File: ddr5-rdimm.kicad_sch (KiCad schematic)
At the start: 34 parts, among them J2 Bus_DDR5_DDR504111002KQ, Q10 BSS138PW, Q11 BSS138PW, Q23 SI7613DN-T1-GE3, Q25 BSS138PW, Q26 BSS138PW, Q27 SI7613DN-T1-GE3, Q9 BSS138PW, SW3 SW_KMR211NGLFS_SMD

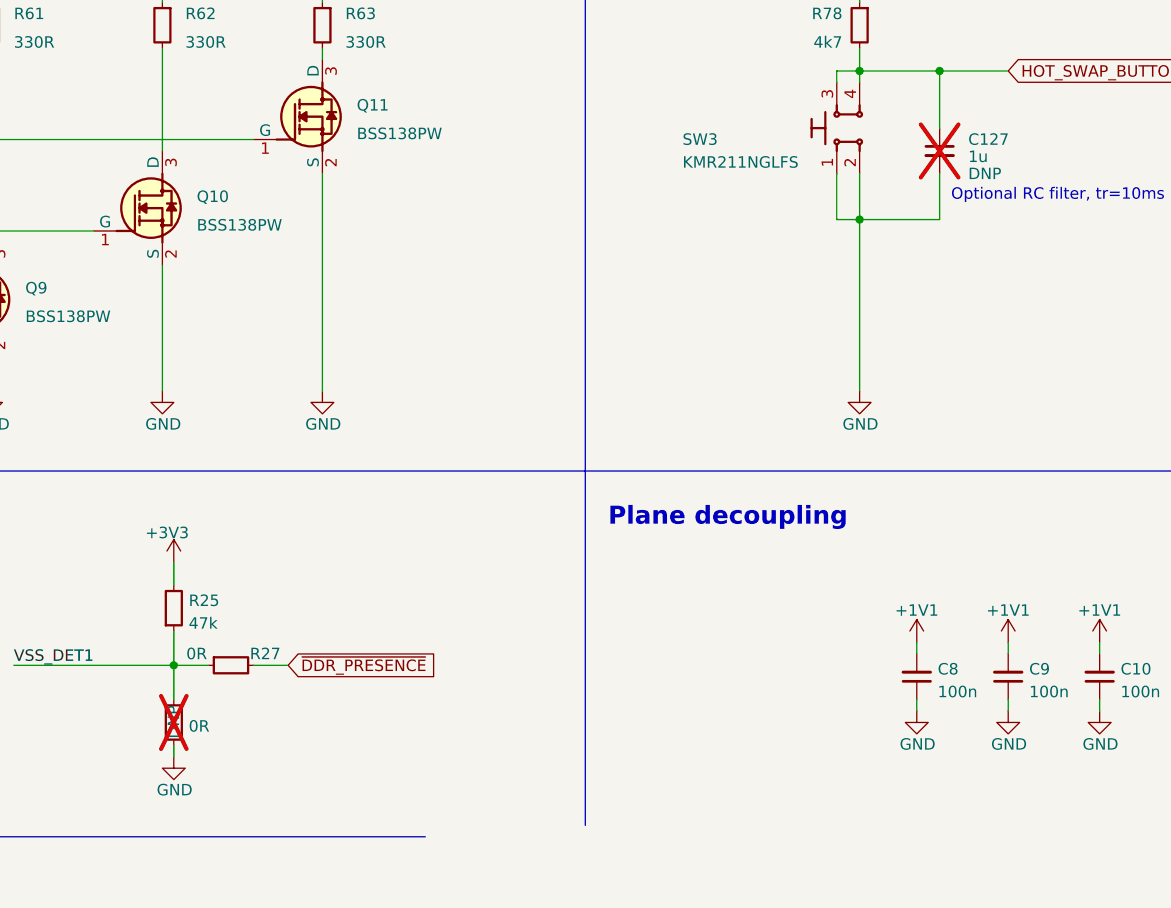
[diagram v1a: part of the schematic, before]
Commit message: [#69629] Fix DNP attributes
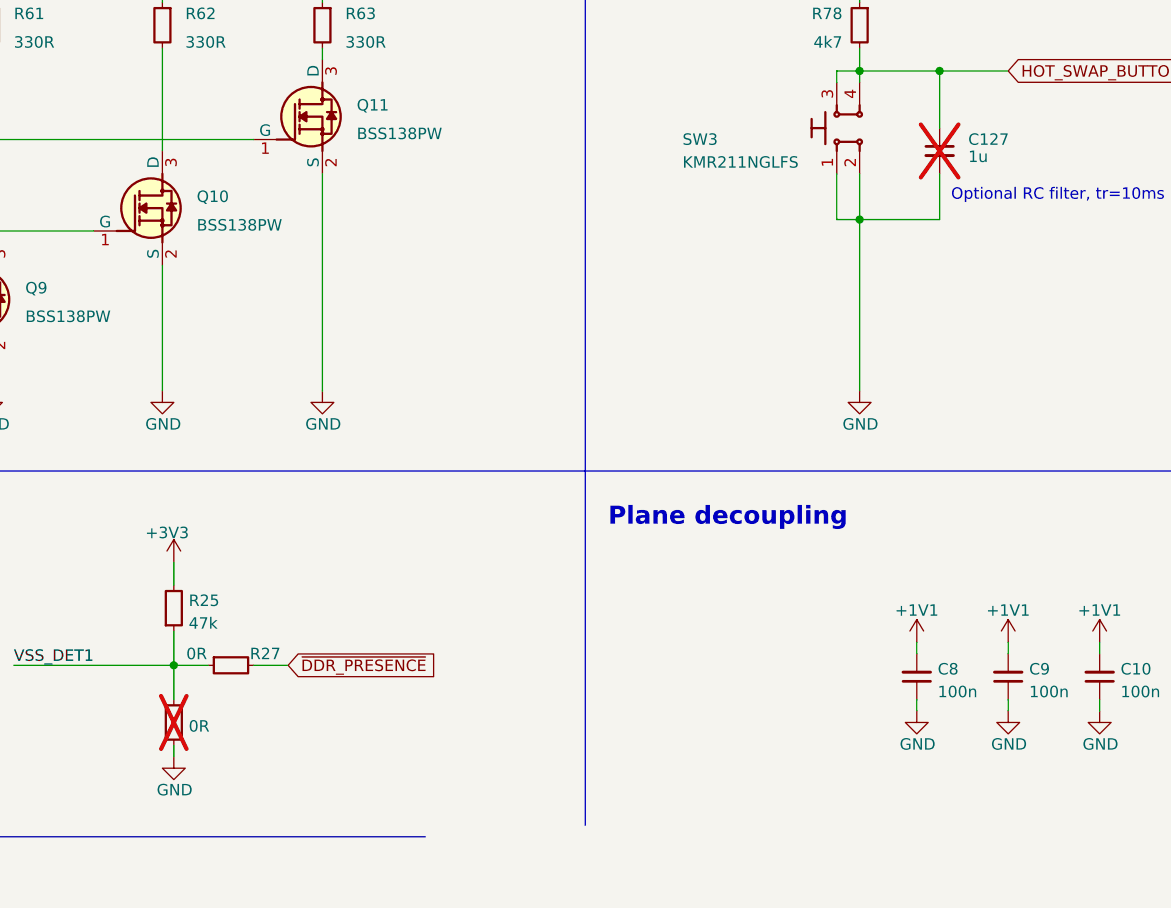
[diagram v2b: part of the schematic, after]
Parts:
- C127, R26: DNP DNP -> (none)

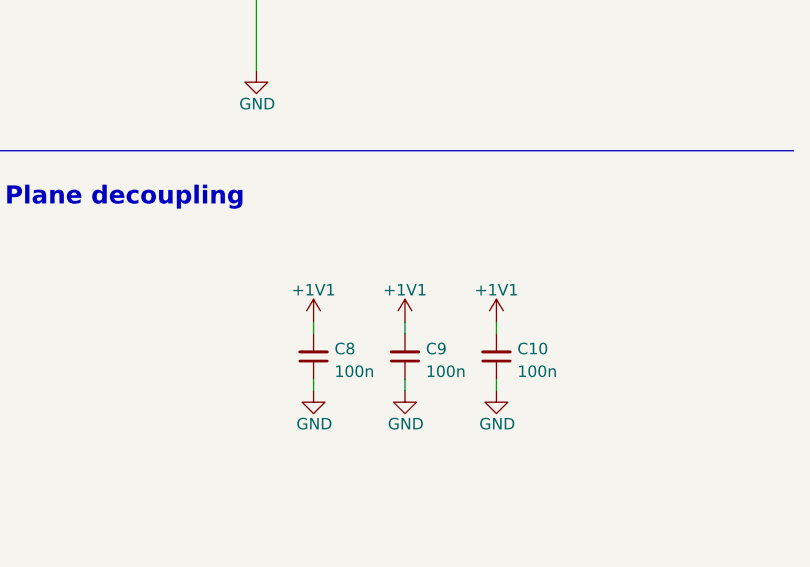
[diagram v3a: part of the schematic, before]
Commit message: [#70235] Improve power supply labels
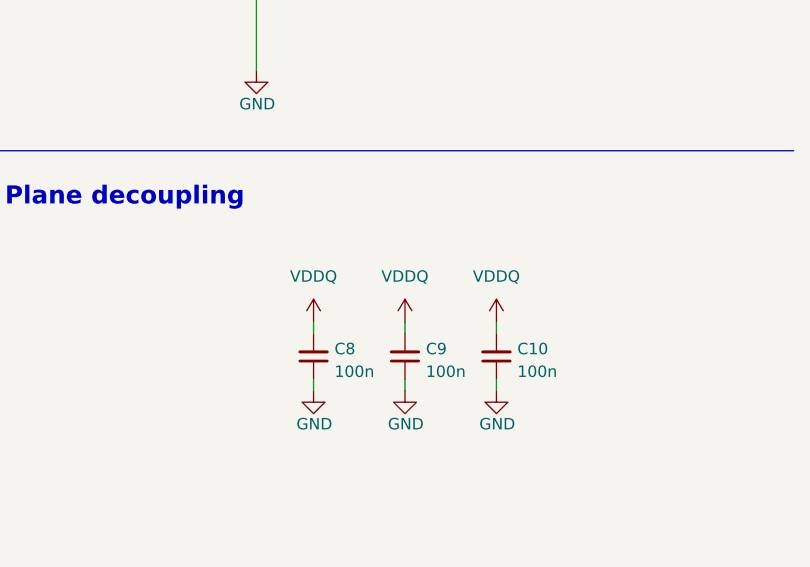
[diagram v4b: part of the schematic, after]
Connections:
- net +1V1 renamed VDDQ
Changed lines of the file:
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@@
 	)
 	(symbol
+		(lib_id "antmicropower:VDD")
+		(at 374.65 232.41 0)
+		(unit 1)
+		(exclude_from_sim no)
+		(in_bom yes)
+		(on_board yes)
+		(dnp no)
+		(fields_autoplaced yes)
+		(property "Reference" "#PWR0117"
+			(at 374.65 236.22 0)
+			(effects
+				(font
+					(size 1.27 1.27)
+				)
+				(hide yes)
+			)
+		)
+		(property "Value" "VDDQ"
+			(at 374.65 227.33 0)
+			(effects
+				(font
+					(size 1.27 1.27)
+				)
+			)
+		)
+		(property "Footprint" ""
+			(at 374.65 232.41 0)
+			(effects
+				(font
+					(size 1.27 1.27)
+				)
+				(hide yes)
+			)
+		)
+		(property "Datasheet" ""
+			(at 374.65 232.41 0)
+			(effects
+				(font
+					(size 1.27 1.27)
+				)
+				(hide yes)
+			)
+		)
+		(property "Description" ""
+			(at 374.65 232.41 0)
+			(effects
+				(font
+					(size 1.27 1.27)
+				)
+				(hide yes)
+			)
+		)
+		(pin "1"
+		)
+		(instances
+			(project "data-center-rdimm-ddr5-tester"
+				(path "/1faa6543-e26a-4449-8bac-ee14b9f19e5f/00000000-0000-0000-0000-000061827943"
+					(reference "#PWR0117")
+					(unit 1)
+				)
+			)
+		)
+	)
+	(symbol
 		(lib_id "antmicroResistors0402:R_330R_0402")
 		(at 270.51 161.29 270)
@@
 	)
 	(symbol
+		(lib_id "antmicropower:VDD")
+		(at 364.49 232.41 0)
+		(unit 1)
+		(exclude_from_sim no)
+		(in_bom yes)
+		(on_board yes)
+		(dnp no)
+		(fields_autoplaced yes)
+		(property "Reference" "#PWR044"
+			(at 364.49 236.22 0)
+			(effects
+				(font
+					(size 1.27 1.27)
+				)
+				(hide yes)
+			)
+		)
+		(property "Value" "VDDQ"
+			(at 364.49 227.33 0)
+			(effects
+				(font
+					(size 1.27 1.27)
+				)
+			)
+		)
+		(property "Footprint" ""
+			(at 364.49 232.41 0)
+			(effects
+				(font
+					(size 1.27 1.27)
+				)
+				(hide yes)
+			)
+		)
+		(property "Datasheet" ""
+			(at 364.49 232.41 0)
+			(effects
+				(font
+					(size 1.27 1.27)
+				)
+				(hide yes)
+			)
+		)
+		(property "Description" ""
+			(at 364.49 232.41 0)
+			(effects
+				(font
+					(size 1.27 1.27)
+				)
+				(hide yes)
+			)
+		)
+		(pin "1"
+		)
+		(instances
+			(project "data-center-rdimm-ddr5-tester"
+				(path "/1faa6543-e26a-4449-8bac-ee14b9f19e5f/00000000-0000-0000-0000-000061827943"
+					(reference "#PWR044")
+					(unit 1)
+				)
+			)
+		)
+	)
+	(symbol
 		(lib_id "antmicropower:GND")
 		(at 248.92 48.26 0)
@@
 	)
 	(symbol
-		(lib_id "antmicropower:+1V1")
-		(at 364.49 232.41 0)
-		(unit 1)
-		(exclude_from_sim no)
-		(in_bom yes)
-		(on_board yes)
-		(dnp no)
-		(fields_autoplaced yes)
-		(property "Reference" "#PWR046"
-			(at 364.49 236.22 0)
-			(effects
-				(font
-					(size 1.27 1.27)
-				)
-				(hide yes)
-			)
-		)
-		(property "Value" "+1V1"
-			(at 364.49 228.854 0)
-			(effects
-				(font
-					(size 1.27 1.27)
-				)
-			)
-		)
-		(property "Footprint" ""
-			(at 364.49 232.41 0)
-			(effects
-				(font
-					(size 1.27 1.27)
-				)
-				(hide yes)
-			)
-		)
-		(property "Datasheet" ""
-			(at 364.49 232.41 0)
-			(effects
-				(font
-					(size 1.27 1.27)
-				)
-				(hide yes)
-			)
-		)
-		(property "Description" ""
-			(at 364.49 232.41 0)
-			(effects
-				(font
-					(size 1.27 1.27)
-				)
-				(hide yes)
-			)
-		)
-		(pin "1"
-		)
-		(instances
-			(project "data-center-rdimm-ddr5-tester"
-				(path "/1faa6543-e26a-4449-8bac-ee14b9f19e5f/00000000-0000-0000-0000-000061827943"
-					(reference "#PWR046")
-					(unit 1)
-				)
-			)
-		)
-	)
-	(symbol
 		(lib_id "antmicropower:GND")
 		(at 281.94 116.84 0)
@@
 	)
 	(symbol
+		(lib_id "antmicropower:VDD")
+		(at 354.33 232.41 0)
+		(unit 1)
+		(exclude_from_sim no)
+		(in_bom yes)
+		(on_board yes)
+		(dnp no)
+		(fields_autoplaced yes)
+		(property "Reference" "#PWR046"
+			(at 354.33 236.22 0)
+			(effects
+				(font
+					(size 1.27 1.27)
+				)
+				(hide yes)
+			)
+		)
+		(property "Value" "VDDQ"
+			(at 354.33 227.33 0)
+			(effects
+				(font
+					(size 1.27 1.27)
+				)
+			)
+		)
+		(property "Footprint" ""
+			(at 354.33 232.41 0)
+			(effects
+				(font
+					(size 1.27 1.27)
+				)
+				(hide yes)
+			)
+		)
+		(property "Datasheet" ""
+			(at 354.33 232.41 0)
+			(effects
+				(font
+					(size 1.27 1.27)
+				)
+				(hide yes)
+			)
+		)
+		(property "Description" ""
+			(at 354.33 232.41 0)
+			(effects
+				(font
+					(size 1.27 1.27)
+				)
+				(hide yes)
+			)
+		)
+		(pin "1"
+		)
+		(instances
+			(project "data-center-rdimm-ddr5-tester"
+				(path "/1faa6543-e26a-4449-8bac-ee14b9f19e5f/00000000-0000-0000-0000-000061827943"
+					(reference "#PWR046")
+					(unit 1)
+				)
+			)
+		)
+	)
+	(symbol
 		(lib_id "antmicroPushbuttonSwitches:SW_KMR211NGLFS_SMD")
 		(at 345.44 180.34 90)
@@
 	)
 	(symbol
-		(lib_id "antmicropower:+1V1")
-		(at 374.65 232.41 0)
-		(unit 1)
-		(exclude_from_sim no)
-		(in_bom yes)
-		(on_board yes)
-		(dnp no)
-		(fields_autoplaced yes)
-		(property "Reference" "#PWR048"
-			(at 374.65 236.22 0)
-			(effects
-				(font
-					(size 1.27 1.27)
-				)
-				(hide yes)
-			)
-		)
-		(property "Value" "+1V1"
-			(at 374.65 228.854 0)
-			(effects
-				(font
-					(size 1.27 1.27)
-				)
-			)
-		)
-		(property "Footprint" ""
-			(at 374.65 232.41 0)
-			(effects
-				(font
-					(size 1.27 1.27)
-				)
-				(hide yes)
-			)
-		)
-		(property "Datasheet" ""
-			(at 374.65 232.41 0)
-			(effects
-				(font
-					(size 1.27 1.27)
-				)
-				(hide yes)
-			)
-		)
-		(property "Description" ""
-			(at 374.65 232.41 0)
-			(effects
-				(font
-					(size 1.27 1.27)
-				)
-				(hide yes)
-			)
-		)
-		(pin "1"
-		)
-		(instances
-			(project "data-center-rdimm-ddr5-tester"
-				(path "/1faa6543-e26a-4449-8bac-ee14b9f19e5f/00000000-0000-0000-0000-000061827943"
-					(reference "#PWR048")
-					(unit 1)
-				)
-			)
-		)
-	)
-	(symbol
 		(lib_id "antmicroTransistorsFETsMOSFETsSingle:BSS138PW")
 		(at 280.67 176.53 0)
@@
 					(unit 1)
 				)
-			)
-		)
-	)
-	(symbol
-		(lib_id "antmicropower:+1V1")
-		(at 354.33 232.41 0)
-		(unit 1)
-		(exclude_from_sim no)
-		(in_bom yes)
-		(on_board yes)
-		(dnp no)
-		(fields_autoplaced yes)
-		(property "Reference" "#PWR044"
-			(at 354.33 236.22 0)
-			(effects
-				(font
-					(size 1.27 1.27)
-				)
-				(hide yes)
-			)
-		)
-		(property "Value" "+1V1"
-			(at 354.33 228.854 0)
-			(effects
-				(font
-					(size 1.27 1.27)
-				)
-			)
-		)
-		(property "Footprint" ""
-			(at 354.33 232.41 0)
-			(effects
-				(font
-					(size 1.27 1.27)
-				)
-				(hide yes)
-			)
-		)
-		(property "Datasheet" ""
-			(at 354.33 232.41 0)
-			(effects
-				(font
-					(size 1.27 1.27)
-				)
-				(hide yes)
-			)
-		)
-		(property "Description" ""
-			(at 354.33 232.41 0)
-			(effects
-				(font
-					(size 1.27 1.27)
-				)
-				(hide yes)
-			)
-		)
-		(pin "1"
-		)
-		(instances
-			(project "data-center-rdimm-ddr5-tester"
-				(path "/1faa6543-e26a-4449-8bac-ee14b9f19e5f/00000000-0000-0000-0000-000061827943"
-					(reference "#PWR044")
-					(unit 1)
-				)
